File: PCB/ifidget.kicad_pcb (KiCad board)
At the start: 2 copper layers, 71.9 x 65.7 mm, 56 parts, among them P1 USB_OTG, P17 DBG_CONN, P2 BatteryHolder, P3 BatteryHolder, P4 BatteryHolder, Q1 Q_PMOS_DSG, SW2 SW_PUSH, SW3 SW_PUSH, SW4 SW_PUSH, U1 74AHC1G125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

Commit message: updates
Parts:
- removed D6: RX, project_footprints:Led_0603
- removed D7: TX, project_footprints:Led_0603
- removed R13, R14: 1k, project_footprints:R_0402_Hand
- added C13: 1uF, project_footprints:C_0402_Hand, F.Cu at (150.6, 84.0)
- added R18: 10k, project_footprints:R_0402_Hand, F.Cu at (125.6, 86.6)
- added R19: 10k, project_footprints:R_0402_Hand, F.Cu at (151.8, 76.0)
- added R20: 10k, project_footprints:R_0402_Hand, F.Cu at (121.6, 81.0)
- added R21: 10k, project_footprints:R_0402_Hand, F.Cu at (149.1, 82.5)
- added R22: 10k, project_footprints:R_0402_Hand, F.Cu at (122.7, 82.9)
- added R23: 10k, project_footprints:R_0402_Hand, F.Cu at (150.2, 80.6)
- added U5: MCP73831T, idlehands_footprints:sot23-5, F.Cu at (108.8, 85.3)
- added U6: TLE4946-2K, idlehands_footprints:SOT23, F.Cu at (125.0, 80.3)
- added U7: TLE4946-2K, idlehands_footprints:SOT23, F.Cu at (147.2, 80.1)
- P17: footprint Pin_Headers:Pin_Header_Straight_2x05_Pitch1.27mm -> idlehands_footprints:Pin_Header_SMD_2x05_Pitch1.27mm
- SW4: footprint Buttons_Switches_SMD:SW_SPST_EVQPE1 -> idlehands_footprints:SOLDER-JUMPER_1-WAY
- moved L1 230.0 mm to (127.5, 47.2), turned to 45 degrees
- moved C7 226.2 mm to (108.9, 82.3), turned to 30 degrees
- moved D1 220.3 mm to (111.5, 83.7), turned to 300 degrees
- moved C1 220.2 mm to (128.0, 50.2), turned to 135 degrees
- moved U1 218.3 mm to (117.1, 85.2), turned to 300 degrees
- moved R5 218.0 mm to (106.0, 83.9), turned to 30 degrees
- moved C12 217.6 mm to (139.8, 41.2), turned to 135 degrees
- moved R2 216.6 mm to (119.5, 90.1), turned to 30 degrees
- moved F1 215.8 mm to (129.8, 58.1)
- moved C9 214.3 mm to (108.8, 91.5), turned to 210 degrees
- moved R3 214.2 mm to (142.8, 44.2), turned to 135 degrees
- moved C6 211.6 mm to (129.8, 59.8)
- moved C10 211.4 mm to (111.9, 86.3), turned to 210 degrees
- moved C3 211.0 mm to (130.3, 52.7), turned to 315 degrees
- moved C5 208.7 mm to (141.2, 42.7), turned to 315 degrees
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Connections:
- net /SD_CS renamed Net-(U2-Pad23)
- net /SPI_MISO renamed Net-(U2-Pad21)
- net IR_EN renamed Net-(U2-Pad22)
- net OUTZ renamed Net-(U2-Pad3)
- D10 pad 1: Net-(D10-Pad1) -> GND
- D11 pad 1: Net-(D11-Pad1) -> GND
- D2 pad 1: Net-(D2-Pad1) -> GND
- D3 pad 1: Net-(D3-Pad1) -> GND
- D4 pad 1: Net-(D4-Pad1) -> GND
- D5 pad 1: Net-(D5-Pad1) -> GND
- D8 pad 1: Net-(D8-Pad1) -> GND
- D9 pad 1: Net-(D9-Pad1) -> GND
- SW2 pad 2: GND -> +3V3
- SW3 pad 2: GND -> +3V3
- U2 pad 11: Net-(U2-Pad11) -> STAT
- U2 pad 26: Net-(U2-Pad26) -> HALL1
- U2 pad 28: Net-(U2-Pad28) -> HALL2
- U4 pad 16: SBATT -> +3V3
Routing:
- net VBATT: track 0.00 -> 173.7 mm, vias 0 -> 1
- net USB_HOST_EN: track 0.00 -> 61.5 mm, vias 0 -> 4
- net STAT: track 0.00 -> 61.4 mm
- net /BUT1: track 0.00 -> 56.7 mm, vias 0 -> 4
- net GND: track 0.00 -> 50.8 mm, vias 0 -> 30
- net +3V3: track 0.00 -> 47.8 mm, vias 0 -> 16
- net DATA: track 0.00 -> 47.7 mm, vias 0 -> 2
- net USB_ID: track 0.00 -> 47.4 mm, vias 0 -> 1
- net LATCH: track 0.00 -> 45.5 mm, vias 0 -> 2
- net HALL1: track 0.00 -> 44.6 mm, vias 0 -> 2
- net VCC: track 0.00 -> 42.7 mm, vias 0 -> 2
- net /BUT2: track 0.00 -> 38.5 mm, vias 0 -> 2
- net VCOM: track 0.00 -> 38.4 mm
- net HALL2: track 0.00 -> 36.4 mm, vias 0 -> 2
- net CLK: track 0.00 -> 35.0 mm, vias 0 -> 2
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
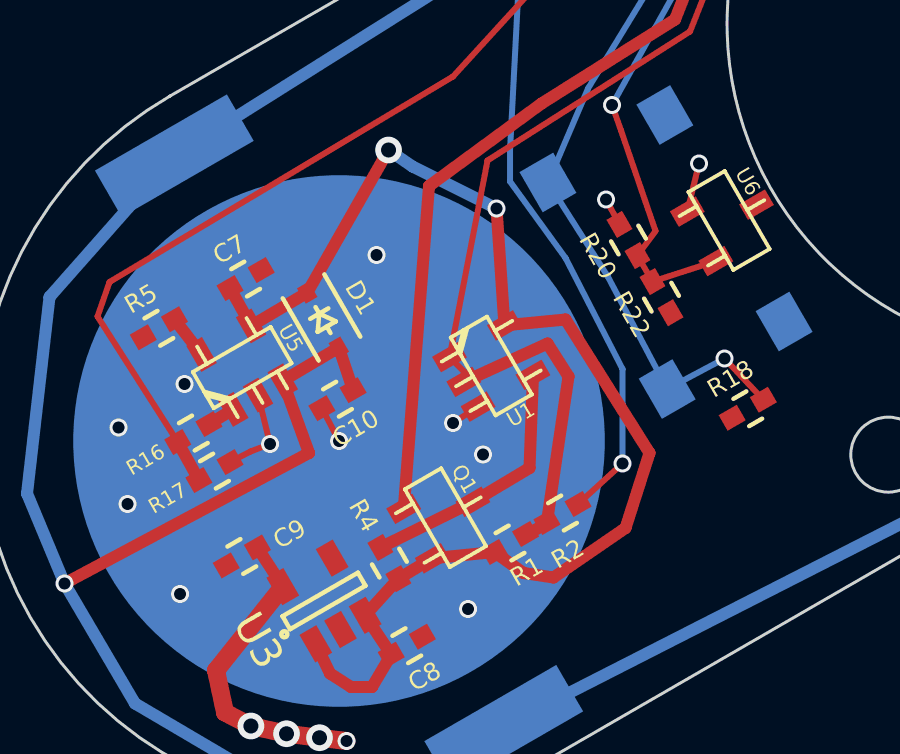
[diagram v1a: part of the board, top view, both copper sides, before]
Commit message: fixed Q1 Pads
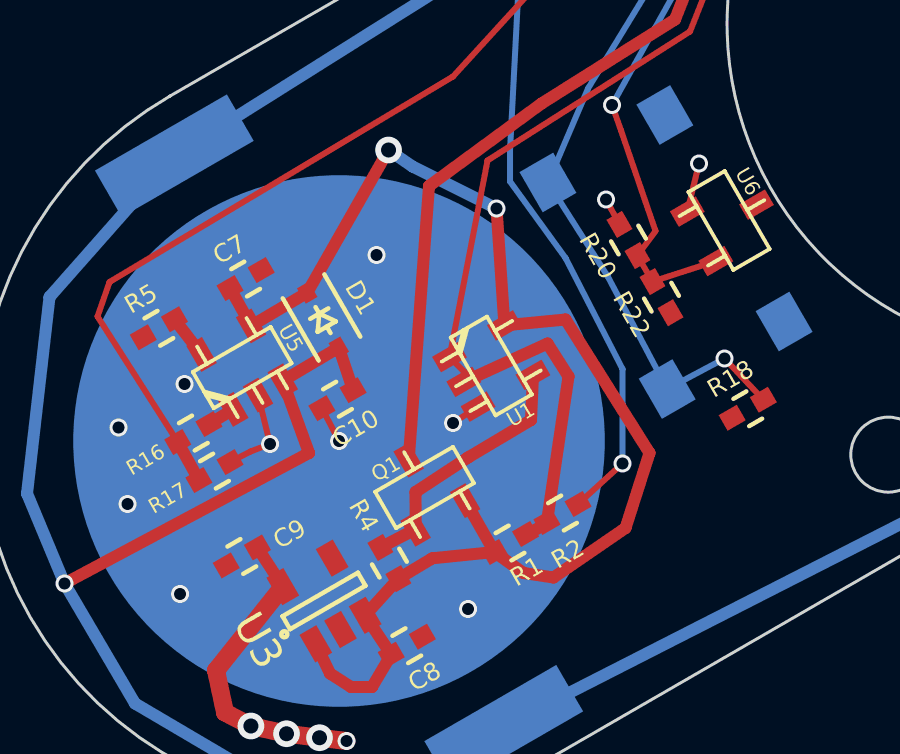
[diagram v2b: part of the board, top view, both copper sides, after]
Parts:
- Q1: footprint project_footprints:SOT23 -> idlehands_footprints:SOT23_Q_PMOS_DSG
- moved Q1 1.23 mm to (114.8, 89.2), turned to 30 degrees
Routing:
- net VCC: track 42.7 -> 44.6 mm
- net VCOM: track 38.4 -> 36.8 mm
- net GND: vias 30 -> 29
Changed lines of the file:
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@@
     (links 144)
     (no_connects 3)
-    (area 99.956934 34.170177 172.012498 99.995177)
+    (area 82.232027 24.3 198.250001 141.234994)
     (thickness 1.6)
     (drawings 33)
-    (tracks 474)
+    (tracks 476)
     (zones 0)
     (modules 62)
@@
   )
   (setup
-    (last_trace_width 0.2)
+    (last_trace_width 0.4)
     (user_trace_width 0.2)
     (user_trace_width 0.4)
@@
     )
   )
-  (module project_footprints:SOT23 (layer F.Cu)
-    (at 115.548658 90.256529 300)
-    (descr SOT23)
-    (fp_text reference Q1 (at -0.81 -1.19 300) (layer F.SilkS)
-      (effects (font (size 0.5 0.5) (thickness 0.125)))
-    )
-    (fp_text value Q_PMOS_DSG (at 0 0.3302 300) (layer F.SilkS) hide
-      (effects (font (size 0.5 0.5) (thickness 0.125)))
-    )
-    (fp_line (start 0.9525 0.6985) (end 0.9525 1.3589) (layer F.SilkS) (width 0.127))
-    (fp_line (start -0.9525 0.6985) (end -0.9525 1.3589) (layer F.SilkS) (width 0.127))
-    (fp_line (start 0 -0.6985) (end 0 -1.3589) (layer F.SilkS) (width 0.127))
-    (fp_line (start -1.4986 -0.6985) (end 1.4986 -0.6985) (layer F.SilkS) (width 0.127))
-    (fp_line (start 1.4986 -0.6985) (end 1.4986 0.6985) (layer F.SilkS) (width 0.127))
-    (fp_line (start 1.4986 0.6985) (end -1.4986 0.6985) (layer F.SilkS) (width 0.127))
-    (fp_line (start -1.4986 0.6985) (end -1.4986 -0.6985) (layer F.SilkS) (width 0.127))
-    (pad 1 smd rect (at -0.9525 1.05664 300) (size 0.59944 1.00076) (layers F.Cu F.Paste F.Mask)
-      (net 7 VCOM))
-    (pad 3 smd rect (at 0 -1.05664 300) (size 0.59944 1.00076) (layers F.Cu F.Paste F.Mask)
-      (net 30 "Net-(Q1-Pad3)"))
-    (pad 2 smd rect (at 0.9525 1.05664 300) (size 0.59944 1.00076) (layers F.Cu F.Paste F.Mask)
-      (net 8 VCC))
-    (model walter/smd_trans/sot23.wrl
-      (at (xyz 0 0 0))
-      (scale (xyz 1 1 1))
-      (rotate (xyz 0 0 0))
-    )
-  )
   (module project_footprints:R_0402_Hand (layer F.Cu)
     (at 117.7 91.1 30)
@@
       (net 1 GND))
   )
+  (module idlehands_footprints:SOT23_Q_PMOS_DSG (layer F.Cu)
+    (at 114.85 89.25 30)
+    (descr SOT23)
+    (fp_text reference Q1 (at -0.81 -1.19 30) (layer F.SilkS)
+      (effects (font (size 0.5 0.5) (thickness 0.125)))
+    )
+    (fp_text value Q_PMOS_DSG (at 0 0.3302 30) (layer F.SilkS) hide
+      (effects (font (size 0.5 0.5) (thickness 0.125)))
+    )
+    (fp_line (start 0.9525 0.6985) (end 0.9525 1.3589) (layer F.SilkS) (width 0.127))
+    (fp_line (start -0.9525 0.6985) (end -0.9525 1.3589) (layer F.SilkS) (width 0.127))
+    (fp_line (start 0 -0.6985) (end 0 -1.3589) (layer F.SilkS) (width 0.127))
+    (fp_line (start -1.4986 -0.6985) (end 1.4986 -0.6985) (layer F.SilkS) (width 0.127))
+    (fp_line (start 1.4986 -0.6985) (end 1.4986 0.6985) (layer F.SilkS) (width 0.127))
+    (fp_line (start 1.4986 0.6985) (end -1.4986 0.6985) (layer F.SilkS) (width 0.127))
+    (fp_line (start -1.4986 0.6985) (end -1.4986 -0.6985) (layer F.SilkS) (width 0.127))
+    (pad 3 smd rect (at -0.9525 1.05664 30) (size 0.59944 1.00076) (layers F.Cu F.Paste F.Mask)
+      (net 30 "Net-(Q1-Pad3)"))
+    (pad 1 smd rect (at 0 -1.05664 30) (size 0.59944 1.00076) (layers F.Cu F.Paste F.Mask)
+      (net 7 VCOM))
+    (pad 2 smd rect (at 0.9525 1.05664 30) (size 0.59944 1.00076) (layers F.Cu F.Paste F.Mask)
+      (net 8 VCC))
+    (model walter/smd_trans/sot23.wrl
+      (at (xyz 0 0 0))
+      (scale (xyz 1 1 1))
+      (rotate (xyz 0 0 0))
+    )
+  )
   (dimension 71.70007 (width 0.3) (layer Cmts.User)
     (gr_text "71.700 mm" (at 135.936049 112.647021 0.07991037986) (layer Cmts.User)
@@
   (via (at 116.3 93.3) (size 0.6) (drill 0.4) (layers F.Cu B.Cu) (net 1))
   (via (at 106.7 92.8) (size 0.6) (drill 0.4) (layers F.Cu B.Cu) (net 1))
-  (via (at 116.8 88.15) (size 0.6) (drill 0.4) (layers F.Cu B.Cu) (net 1))
   (via (at 113.25 81.5) (size 0.6) (drill 0.4) (layers F.Cu B.Cu) (net 1))
   (via (at 106.85 85.8) (size 0.6) (drill 0.4) (layers F.Cu B.Cu) (net 1))
@@
   (segment (start 138.899138 44.147309) (end 140.795711 42.250736) (width 0.2) (layer F.Cu) (net 6))
   (segment (start 140.795711 42.250736) (end 140.825736 42.250736) (width 0.2) (layer F.Cu) (net 6))
+  (segment (start 115 79.2) (end 114.32168 88.334923) (width 0.4) (layer F.Cu) (net 7))
   (segment (start 129.05 63.6) (end 129.15 59.825) (width 0.4) (layer F.Cu) (net 7))
   (segment (start 126.35 65.7) (end 129.05 63.6) (width 0.4) (layer F.Cu) (net 7))
@@
   (segment (start 118.75 76.45) (end 123.2 73.65) (width 0.4) (layer F.Cu) (net 7))
   (segment (start 115 79.2) (end 118.75 76.45) (width 0.4) (layer F.Cu) (net 7))
-  (segment (start 114.157331 89.95996) (end 115 79.2) (width 0.4) (layer F.Cu) (net 7))
   (segment (start 128.453 58.15) (end 128.453 59.128) (width 0.4) (layer F.Cu) (net 7))
   (segment (start 128.453 59.128) (end 129.15 59.825) (width 0.4) (layer F.Cu) (net 7))
+  (segment (start 116.203209 89.688827) (end 117.180385 91.4) (width 0.4) (layer F.Cu) (net 8))
   (segment (start 114.45 78.55) (end 113.65 78) (width 0.4) (layer B.Cu) (net 8))
   (segment (start 117.25 79.95) (end 114.45 78.55) (width 0.4) (layer B.Cu) (net 8))
@@
   (segment (start 138.55 38.925) (end 138.55 42.375127) (width 0.2) (layer F.Cu) (net 29))
   (segment (start 138.55 42.375127) (end 137.838478 43.086649) (width 0.2) (layer F.Cu) (net 29))
-  (segment (start 113.379348 91.249173) (end 116.463735 89.728209) (width 0.4) (layer F.Cu) (net 30))
-  (segment (start 118.35 88.6) (end 116.463735 89.728209) (width 0.4) (layer F.Cu) (net 30))
-  (segment (start 118.466327 85.496569) (end 118.35 88.6) (width 0.4) (layer F.Cu) (net 30))
+  (segment (start 118.4 87) (end 118.466327 85.496569) (width 0.4) (layer F.Cu) (net 30))
+  (segment (start 116.3 88.25) (end 118.4 87) (width 0.4) (layer F.Cu) (net 30))
+  (segment (start 114.55 89.4) (end 116.3 88.25) (width 0.4) (layer F.Cu) (net 30))
+  (segment (start 114.553431 90.641327) (end 114.55 89.4) (width 0.4) (layer F.Cu) (net 30))
+  (segment (start 113.379348 91.249173) (end 114.553431 90.641327) (width 0.4) (layer F.Cu) (net 30))
   (segment (start 123.647782 66.1) (end 124.1 52.85) (width 0.2) (layer F.Cu) (net 31))
   (segment (start 123 67.1) (end 123.647782 66.1) (width 0.2) (layer F.Cu) (net 31))

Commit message: fixes to power and listed issues
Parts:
- added D6: LED, idlehands_footprints:Led_0603, F.Cu at (106.0, 87.5)
- added G***: LOGO, idlehands_footprints:OSHLogo, F.Cu at (119.0, 95.1)
- added G***: LOGO, idlehands_footprints:IdlehandsdevLogo, F.Cu at (125.0, 91.8)
- added Q2: 2N7002, TO_SOT_Packages_SMD:SOT-23, F.Cu at (147.8, 90.0)
- added R13: 100k, project_footprints:R_0402_Hand, F.Cu at (145.7, 88.6)
- added R14: 1K, project_footprints:R_0402_Hand, F.Cu at (107.8, 88.0)
- moved R17 8.50 mm to (109.0, 80.3), turned to 120 degrees
- moved R16 8.41 mm to (110.2, 79.6), turned to 300 degrees
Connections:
- R16 pad 2: Net-(R16-Pad2) -> VCC
- U2 pad 23: Net-(U2-Pad23) -> HALLSW
- U5 pad 1: Net-(R16-Pad2) -> Net-(R14-Pad1)
- U6 pad 3: GND -> Net-(Q2-Pad3)
- U7 pad 3: GND -> Net-(Q2-Pad3)
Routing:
- net HALLSW: track 0.00 -> 59.0 mm, vias 0 -> 2
- net Net-(Q2-Pad3): track 0.00 -> 36.7 mm
- net +3V3: track 47.8 -> 71.0 mm, vias 16 -> 19
- net STAT: track 61.4 -> 48.6 mm
- net VCC: track 44.6 -> 52.0 mm
- net GND: track 50.8 -> 54.6 mm, vias 29 -> 27
- net HALL1: track 44.6 -> 48.1 mm
- net /BUT1: track 56.7 -> 59.1 mm
- net Net-(R14-Pad1): track 0.00 -> 1.95 mm
- net Net-(D6-Pad1): track 0.00 -> 1.25 mm
- net Net-(R16-Pad2): track 0.95 -> 0.00 mm

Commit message: Small fix
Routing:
- net GND: track 54.6 -> 55.8 mm
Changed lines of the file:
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@@
     (links 151)
     (no_connects 5)
-    (area 99.956934 34.170177 172.012498 99.995177)
+    (area 82.232027 24.3 198.250001 141.234994)
     (thickness 1.6)
     (drawings 33)
-    (tracks 536)
+    (tracks 537)
     (zones 0)
     (modules 68)
@@
   (gr_line (start 100 100) (end 100 65.6) (layer Dwgs.User) (width 0.1))
   (gr_line (start 100 100) (end 198.2 100) (layer Dwgs.User) (width 0.1))
+  (segment (start 109.406078 82) (end 109.3 80.8) (width 0.2) (layer F.Cu) (net 1))
   (segment (start 134.7 56.75) (end 131.6 52.45) (width 0.2) (layer B.Cu) (net 1))
   (via (at 162.9 79.95) (size 0.6) (drill 0.4) (layers F.Cu B.Cu) (net 1))
